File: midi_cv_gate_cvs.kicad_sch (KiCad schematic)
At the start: 72 parts, among them U20 LM358, U21 LM358, U22 LM358, U23 LM358, U24 LM358, U25 LM358, U26 LM358, U27 LM358

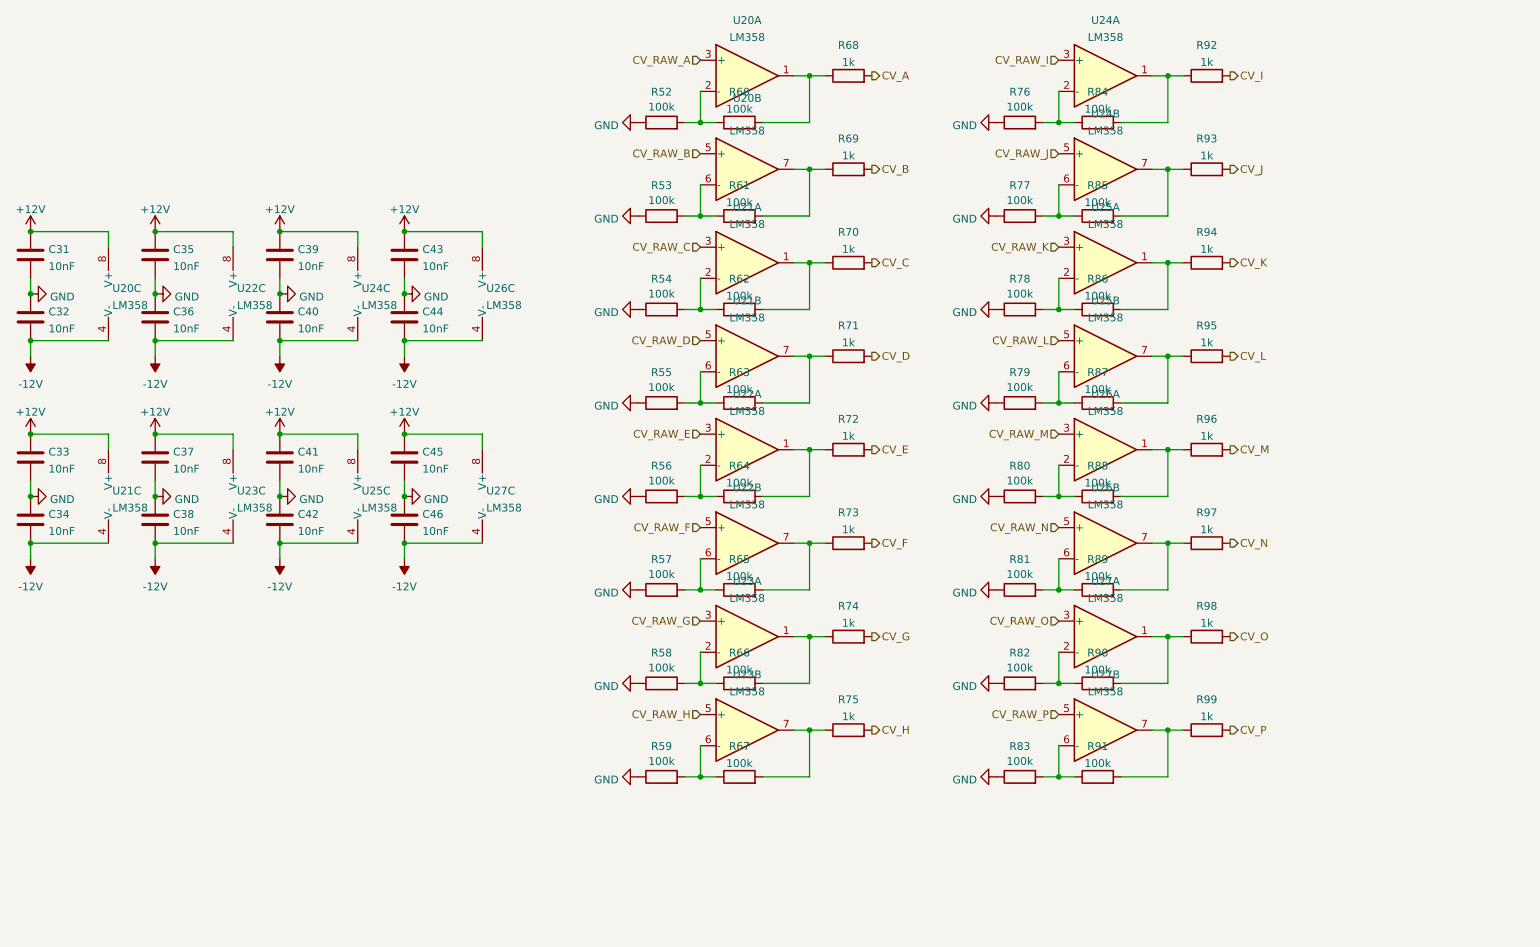
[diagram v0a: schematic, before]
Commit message: Replace soic-14 with dip 14 for DACs, add pulldowns on opamp inputs
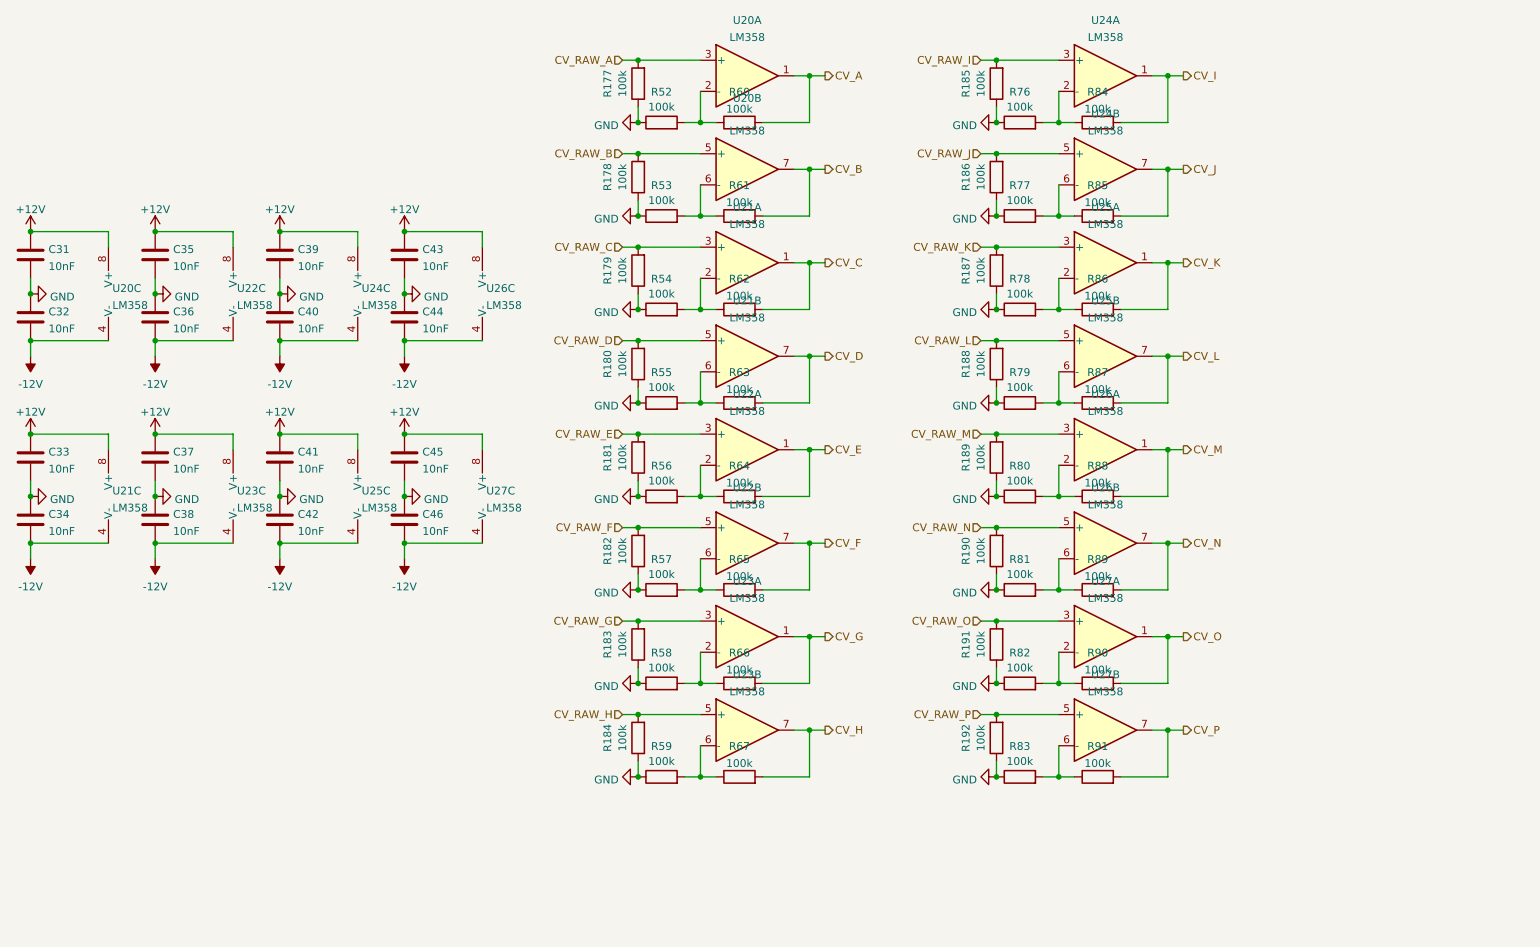
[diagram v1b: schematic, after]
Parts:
- removed R68, R69, R70, R71, R72, R73, R74, R75, R92, R93, R94, R95, R96, R97, R98, R99: 1k, Resistor_SMD:R_1206_3216Metric_Pad1.30x1.75mm_HandSolder, symbol Device:R
- added R177, R178, R179, R180, R181, R182, R183, R184, R185, R186, R187, R188, R189, R190, R191, R192: 100k, Resistor_SMD:R_1206_3216Metric_Pad1.30x1.75mm_HandSolder, symbol Device:R
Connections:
- net CV_A: now also R60.2, U20.1
- net CV_B: now also R61.2, U20.7
- net CV_C: now also R62.2, U21.1
- net CV_D: now also R63.2, U21.7
- net CV_E: now also R64.2, U22.1
- net CV_F: now also R65.2, U22.7
- net CV_G: now also R66.2, U23.1
- net CV_H: now also R67.2, U23.7
- net CV_I: now also R84.2, U24.1
- net CV_J: now also R85.2, U24.7
- net CV_K: now also R86.2, U25.1
- net CV_L: now also R87.2, U25.7
- net CV_M: now also R88.2, U26.1
- net CV_N: now also R89.2, U26.7
- net CV_O: now also R90.2, U27.1
- net CV_P: now also R91.2, U27.7
- net CV_RAW_A: now also R177.2
- net CV_RAW_B: now also R178.2
- net CV_RAW_C: now also R179.2
- net CV_RAW_D: now also R180.2
- net CV_RAW_E: now also R181.2
- net CV_RAW_F: now also R182.2
- net CV_RAW_G: now also R183.2
- net CV_RAW_H: now also R184.2
- net CV_RAW_I: now also R185.2
- net CV_RAW_J: now also R186.2
- net CV_RAW_K: now also R187.2
- net CV_RAW_L: now also R188.2
- net CV_RAW_M: now also R189.2
- net CV_RAW_N: now also R190.2
- net CV_RAW_O: now also R191.2
- net CV_RAW_P: now also R192.2
- net GND: now also R177.1, R178.1, R179.1, R180.1, R181.1, R182.1, R183.1, R184.1, R185.1, R186.1, R187.1, R188.1, R189.1, R190.1, R191.1, R192.1

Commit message: Fixed alignment of jacks and LEDs
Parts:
- renumbered C31 to C1, C35 to C12, C36 to C15, C37 to C17, C38 to C20, C39 to C23, C40 to C26, C41 to C29, C42 to C32, C43 to C34, C44 to C36, C45 to C39, C46 to C40, C32 to C5, C33 to C6, C34 to C9, R187 to R106, R60 to R11, R52 to R12, R63 to R15, R55 to R16, R188 to R160, R89 to R167, R81 to R168, R88 to R169, R80 to R170, R189 to R171, R190 to R172, R91 to R179, R83 to R180, R90 to R181, R82 to R182, R191 to R184, R192 to R185, R179 to R19, R180 to R28, R62 to R31, R54 to R32, R65 to R35, R57 to R36, R181 to R39, R182 to R40, R64 to R41, R56 to R42, R61 to R5, R67 to R54, R59 to R55, R66 to R57, R183 to R59, R53 to R6, R184 to R60, R85 to R66, R77 to R67, R177 to R7, R84 to R78, R76 to R79, R178 to R8, R185 to R80, R186 to R81, R87 to R88, R79 to R89, R86 to R90, R78 to R91, U20 to U103, U21 to U106, U22 to U110, U23 to U112, U24 to U115, U25 to U118, U26 to U121, U27 to U125

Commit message: Cleanups and title blocks
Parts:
- renumbered R28 to R20, R31 to R23, R32 to R24, R35 to R27, R36 to R28, R39 to R31, R40 to R32, R41 to R33, R42 to R34, R54 to R38, R55 to R39, R57 to R41, R58 to R42, R59 to R43, R60 to R44, R66 to R50, R67 to R51, R78 to R54, R79 to R55, R80 to R56, R81 to R57, R88 to R64, R89 to R65, R90 to R66, R91 to R67, R106 to R68, R160 to R69, R167 to R76, R168 to R77, R169 to R78, R170 to R79, R171 to R80, R172 to R81, R179 to R88, R180 to R89, R181 to R90, R182 to R91, R184 to R93, R185 to R94
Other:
- note added: "Gain 2.0"
- note added: "Output Simulation https://tinyurl.com/y5wb9wkh"
- company: (none) -> RobotDialogs
- title: (none) -> Eurorack MIDI 16x16 CV Gate
- moved on the sheet: C1, C12, C15, C17, C20, C23, C26, C29, C32, C34, C36, C39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
